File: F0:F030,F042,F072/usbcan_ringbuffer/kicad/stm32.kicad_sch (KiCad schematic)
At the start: 59 parts, among them J1 Screw_Terminal_01x03, J10 SDA, J11 PB0, J12 PB1, J13 PB4, J14 PB5, J15 PB2, J16 PB3, J17 GND, J18 GND, J19 +3.3V, J2 SCK, J20 +5V, J21 PA0, J22 PA1, J23 PA2, J24 PA3, J25 PB10, J26 PB11, J27 PB12, J28 PB13, J29 PB14, J3 SWDetc, J30 PA4, J31 GND, J4 USB_B, J5 MISO, J6 MOSI, J7 TX, J8 RX, J9 SCL, P1 Hole, P2 Hole, P3 Hole, P4 Hole, Q1 B0505S, SW1 SW_DIP_x01, U1 LM1117-3.3, U2 USBLC6-2SC6, U3 STM32F072C8Tx, U4 ISO1050DUB

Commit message: fixed bug with usblc6 on usbcan
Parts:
- removed J27: PB12, TestPoint:TestPoint_THTPad_1.5x1.5mm_Drill0.7mm, symbol Connector:Conn_01x01_Female
- removed J28: PB13, TestPoint:TestPoint_THTPad_1.5x1.5mm_Drill0.7mm, symbol Connector:Conn_01x01_Female
- removed J29: PB14, TestPoint:TestPoint_THTPad_1.5x1.5mm_Drill0.7mm, symbol Connector:Conn_01x01_Female
- removed J30: PA4, TestPoint:TestPoint_THTPad_1.5x1.5mm_Drill0.7mm, symbol Connector:Conn_01x01_Female
- removed J31: GND, TestPoint:TestPoint_THTPad_1.5x1.5mm_Drill0.7mm, symbol Connector:Conn_01x01_Female
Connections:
- net +5V: now also U2.5 (VBUS); no longer U2.2 (GND)
- net GND: now also U2.2 (GND); no longer U2.5 (VBUS)
- net at R3.2: now also U2.4 (I/O2); no longer U2.1 (I/O1)
- net at R4.2: now also U2.6 (I/O1); no longer U2.3 (I/O2)
- net at U3.32 (PA11): now also U2.3 (I/O2); no longer U2.6 (I/O1)
- net at U3.33 (PA12): now also U2.1 (I/O1); no longer U2.4 (I/O2)
- no-connect marks 10 -> 14
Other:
- moved on the sheet: U2
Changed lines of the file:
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@@
   (junction (at 18.161 84.328) (diameter 0) (color 0 0 0 0)
   )
-  (junction (at 102.108 151.257) (diameter 0) (color 0 0 0 0)
+  (junction (at 182.118 138.303) (diameter 0) (color 0 0 0 0)
   )
   (junction (at 118.618 149.098) (diameter 0) (color 0 0 0 0)
@@
   (junction (at 197.104 123.063) (diameter 0) (color 0 0 0 0)
   )
+  (no_connect (at 105.918 138.938))
+  (no_connect (at 105.918 136.398))
   (no_connect (at 105.918 98.298))
   (no_connect (at 138.938 144.018))
@@
   (no_connect (at 105.918 95.758))
   (no_connect (at 105.918 88.138))
+  (no_connect (at 105.918 141.478))
   (no_connect (at 323.85 187.198))
+  (no_connect (at 138.938 116.078))
   (no_connect (at 105.918 90.678))
   (no_connect (at 323.85 193.548))
@@
     (stroke (width 0) (type default) (color 0 0 0 0))
   )
-  (wire (pts (xy 102.108 149.479) (xy 102.108 151.257))
-    (stroke (width 0) (type default) (color 0 0 0 0))
-  )
   (polyline (pts (xy 68.326 45.212) (xy 68.326 14.478))
     (stroke (width 0) (type default) (color 0 0 0 0))
@@
   )
   (label "LED0" (at 105.918 144.018 180)
-    (effects (font (size 1.2 1.2)) (justify right bottom))
+    (effects (font (size 1.524 1.524)) (justify right bottom))
   )
   (label "LED1" (at 21.717 65.659 180)
@@
   )
   (label "CAN_Rx" (at 105.918 126.238 180)
-    (effects (font (size 1.2 1.2)) (justify right bottom))
+    (effects (font (size 1.524 1.524)) (justify right bottom))
   )
   (label "CAN_Tx" (at 85.979 29.083 180)
@@
   )
   (label "LED1" (at 138.938 126.238 0)
-    (effects (font (size 1.2 1.2)) (justify left bottom))
+    (effects (font (size 1.524 1.524)) (justify left bottom))
   )
   (label "BOOT0" (at 136.779 34.925 180)
@@
     (pin "1")
     (pin "2")
+  )
+  (symbol (lib_id "stm32-rescue:PWR_FLAG") (at 182.118 138.303 180) (unit 1)
+    (in_bom yes) (on_board yes)
+    (property "Reference" "#FLG01" (id 0) (at 182.118 140.716 0)
+      (effects (font (size 1.27 1.27)) hide)
+    )
+    (property "Value" "PWR_FLAG" (id 1) (at 182.118 142.875 0)
+      (effects (font (size 1.27 1.27)) hide)
+    )
+    (property "Footprint" "" (id 2) (at 182.118 138.303 0))
+    (property "Datasheet" "" (id 3) (at 182.118 138.303 0))
+    (pin "1")
   )
   (symbol (lib_id "stm32-rescue:R") (at 100.076 86.868 180) (unit 1)
@@
     (pin "1")
   )
-  (symbol (lib_id "Power_Protection:USBLC6-2SC6") (at 167.64 132.969 90) (mirror x) (unit 1)
-    (in_bom yes) (on_board yes)
-    (property "Reference" "U2" (id 0) (at 167.513 117.856 90))
-    (property "Value" "USBLC6-2SC6" (id 1) (at 166.497 120.269 90))
-    (property "Footprint" "Package_TO_SOT_SMD:SOT-23-6_Handsoldering" (id 2) (at 180.34 132.969 0)
-      (effects (font (size 1.27 1.27)) hide)
-    )
-    (property "Datasheet" "https://www.st.com/resource/en/datasheet/usblc6-2.pdf" (id 3) (at 158.75 138.049 0)
+  (symbol (lib_id "Power_Protection:USBLC6-2SC6") (at 167.64 132.969 270) (mirror x) (unit 1)
+    (in_bom yes) (on_board yes)
+    (property "Reference" "U2" (id 0) (at 167.767 148.082 90))
+    (property "Value" "USBLC6-2SC6" (id 1) (at 168.783 145.669 90))
+    (property "Footprint" "Package_TO_SOT_SMD:SOT-23-6_Handsoldering" (id 2) (at 154.94 132.969 0)
+      (effects (font (size 1.27 1.27)) hide)
+    )
+    (property "Datasheet" "https://www.st.com/resource/en/datasheet/usblc6-2.pdf" (id 3) (at 176.53 127.889 0)
       (effects (font (size 1.27 1.27)) hide)
     )
@@
     (pin "1")
   )
-  (symbol (lib_id "Connector:Conn_01x01_Female") (at 100.838 138.938 180) (unit 1)
-    (in_bom yes) (on_board yes)
-    (property "Reference" "J28" (id 0) (at 100.1268 139.7727 0)
-      (effects (font (size 1.27 1.27)) (justify left) hide)
-    )
-    (property "Value" "PB13" (id 1) (at 100.711 138.938 0)
-      (effects (font (size 1.27 1.27)) (justify left))
-    )
-    (property "Footprint" "TestPoint:TestPoint_THTPad_1.5x1.5mm_Drill0.7mm" (id 2) (at 100.838 138.938 0)
-      (effects (font (size 1.27 1.27)) hide)
-    )
-    (property "Datasheet" "~" (id 3) (at 100.838 138.938 0)
-      (effects (font (size 1.27 1.27)) hide)
-    )
-    (pin "1")
-  )
   (symbol (lib_id "Connector:Conn_01x01_Female") (at 144.018 131.318 0) (unit 1)
     (in_bom yes) (on_board yes)
@@
     (pin "1")
   )
-  (symbol (lib_id "Connector:Conn_01x01_Female") (at 144.018 116.078 0) (unit 1)
-    (in_bom yes) (on_board yes)
-    (property "Reference" "J30" (id 0) (at 144.7292 115.2433 0)
-      (effects (font (size 1.27 1.27)) (justify left) hide)
-    )
-    (property "Value" "PA4" (id 1) (at 144.145 116.078 0)
-      (effects (font (size 1.27 1.27)) (justify left))
-    )
-    (property "Footprint" "TestPoint:TestPoint_THTPad_1.5x1.5mm_Drill0.7mm" (id 2) (at 144.018 116.078 0)
-      (effects (font (size 1.27 1.27)) hide)
-    )
-    (property "Datasheet" "~" (id 3) (at 144.018 116.078 0)
-      (effects (font (size 1.27 1.27)) hide)
-    )
-    (pin "1")
-  )
-  (symbol (lib_id "Connector:Conn_01x01_Female") (at 100.838 141.478 180) (unit 1)
-    (in_bom yes) (on_board yes)
-    (property "Reference" "J29" (id 0) (at 100.1268 142.3127 0)
-      (effects (font (size 1.27 1.27)) (justify left) hide)
-    )
-    (property "Value" "PB14" (id 1) (at 100.711 141.478 0)
-      (effects (font (size 1.27 1.27)) (justify left))
-    )
-    (property "Footprint" "TestPoint:TestPoint_THTPad_1.5x1.5mm_Drill0.7mm" (id 2) (at 100.838 141.478 0)
-      (effects (font (size 1.27 1.27)) hide)
-    )
-    (property "Datasheet" "~" (id 3) (at 100.838 141.478 0)
-      (effects (font (size 1.27 1.27)) hide)
-    )
-    (pin "1")
-  )
   (symbol (lib_id "Connector:Conn_01x01_Female") (at 144.018 118.618 0) (unit 1)
     (in_bom yes) (on_board yes)
@@
     )
     (property "Datasheet" "~" (id 3) (at 100.838 131.318 0)
-      (effects (font (size 1.27 1.27)) hide)
-    )
-    (pin "1")
-  )
-  (symbol (lib_id "Connector:Conn_01x01_Female") (at 100.838 136.398 180) (unit 1)
-    (in_bom yes) (on_board yes)
-    (property "Reference" "J27" (id 0) (at 100.1268 137.2327 0)
-      (effects (font (size 1.27 1.27)) (justify left) hide)
-    )
-    (property "Value" "PB12" (id 1) (at 100.711 136.398 0)
-      (effects (font (size 1.27 1.27)) (justify left))
-    )
-    (property "Footprint" "TestPoint:TestPoint_THTPad_1.5x1.5mm_Drill0.7mm" (id 2) (at 100.838 136.398 0)
-      (effects (font (size 1.27 1.27)) hide)
-    )
-    (property "Datasheet" "~" (id 3) (at 100.838 136.398 0)
-      (effects (font (size 1.27 1.27)) hide)
-    )
-    (pin "1")
-  )
-  (symbol (lib_id "Connector:Conn_01x01_Female") (at 97.028 149.479 180) (unit 1)
-    (in_bom yes) (on_board yes)
-    (property "Reference" "J31" (id 0) (at 96.3168 150.3137 0)
-      (effects (font (size 1.27 1.27)) (justify left) hide)
-    )
-    (property "Value" "GND" (id 1) (at 96.901 149.479 0)
-      (effects (font (size 1.27 1.27)) (justify left))
-    )
-    (property "Footprint" "TestPoint:TestPoint_THTPad_1.5x1.5mm_Drill0.7mm" (id 2) (at 97.028 149.479 0)
-      (effects (font (size 1.27 1.27)) hide)
-    )
-    (property "Datasheet" "~" (id 3) (at 97.028 149.479 0)
       (effects (font (size 1.27 1.27)) hide)
     )
@@
   )
   (symbol_instances
+    (path "/00000000-0000-0000-0000-0000590cee5e"
+      (reference "#FLG01") (unit 1) (value "PWR_FLAG") (footprint "")
+    )
     (path "/00000000-0000-0000-0000-000058c45269"
       (reference "#PWR01") (unit 1) (value "+5V") (footprint "")
@@
       (reference "J26") (unit 1) (value "PB11") (footprint "TestPoint:TestPoint_THTPad_1.5x1.5mm_Drill0.7mm")
     )
-    (path "/6acab1d7-5134-4383-9218-96f6aed30a0e"
-      (reference "J27") (unit 1) (value "PB12") (footprint "TestPoint:TestPoint_THTPad_1.5x1.5mm_Drill0.7mm")
-    )
-    (path "/27c8ca30-700e-4f17-a521-c0a04628cef7"
-      (reference "J28") (unit 1) (value "PB13") (footprint "TestPoint:TestPoint_THTPad_1.5x1.5mm_Drill0.7mm")
-    )
-    (path "/5139d6c7-f281-4162-939d-b58b280c93c5"
-      (reference "J29") (unit 1) (value "PB14") (footprint "TestPoint:TestPoint_THTPad_1.5x1.5mm_Drill0.7mm")
-    )
-    (path "/4665fb37-cc57-492c-a310-df271b1f2833"
-      (reference "J30") (unit 1) (value "PA4") (footprint "TestPoint:TestPoint_THTPad_1.5x1.5mm_Drill0.7mm")
-    )
-    (path "/757390d4-03a1-4ffc-88c1-d08120dcec23"
-      (reference "J31") (unit 1) (value "GND") (footprint "TestPoint:TestPoint_THTPad_1.5x1.5mm_Drill0.7mm")
-    )
     (path "/00000000-0000-0000-0000-000059143415"

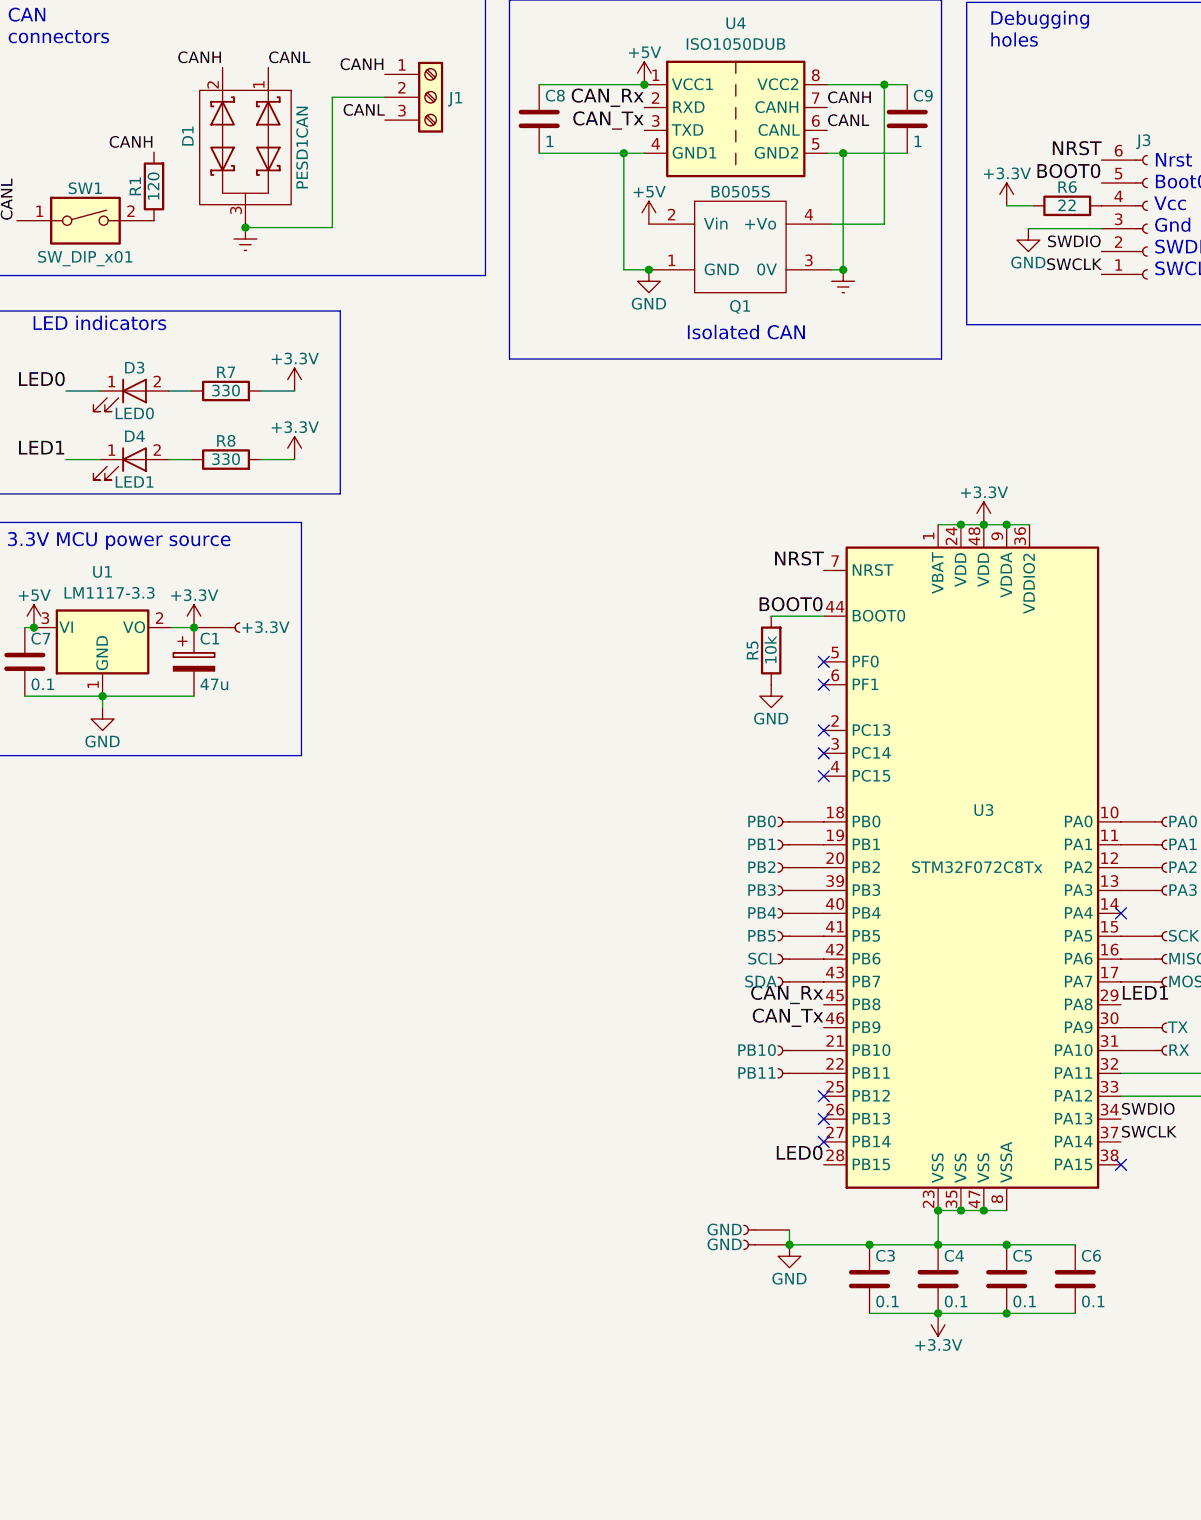
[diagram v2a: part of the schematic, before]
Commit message: -> kicad 8
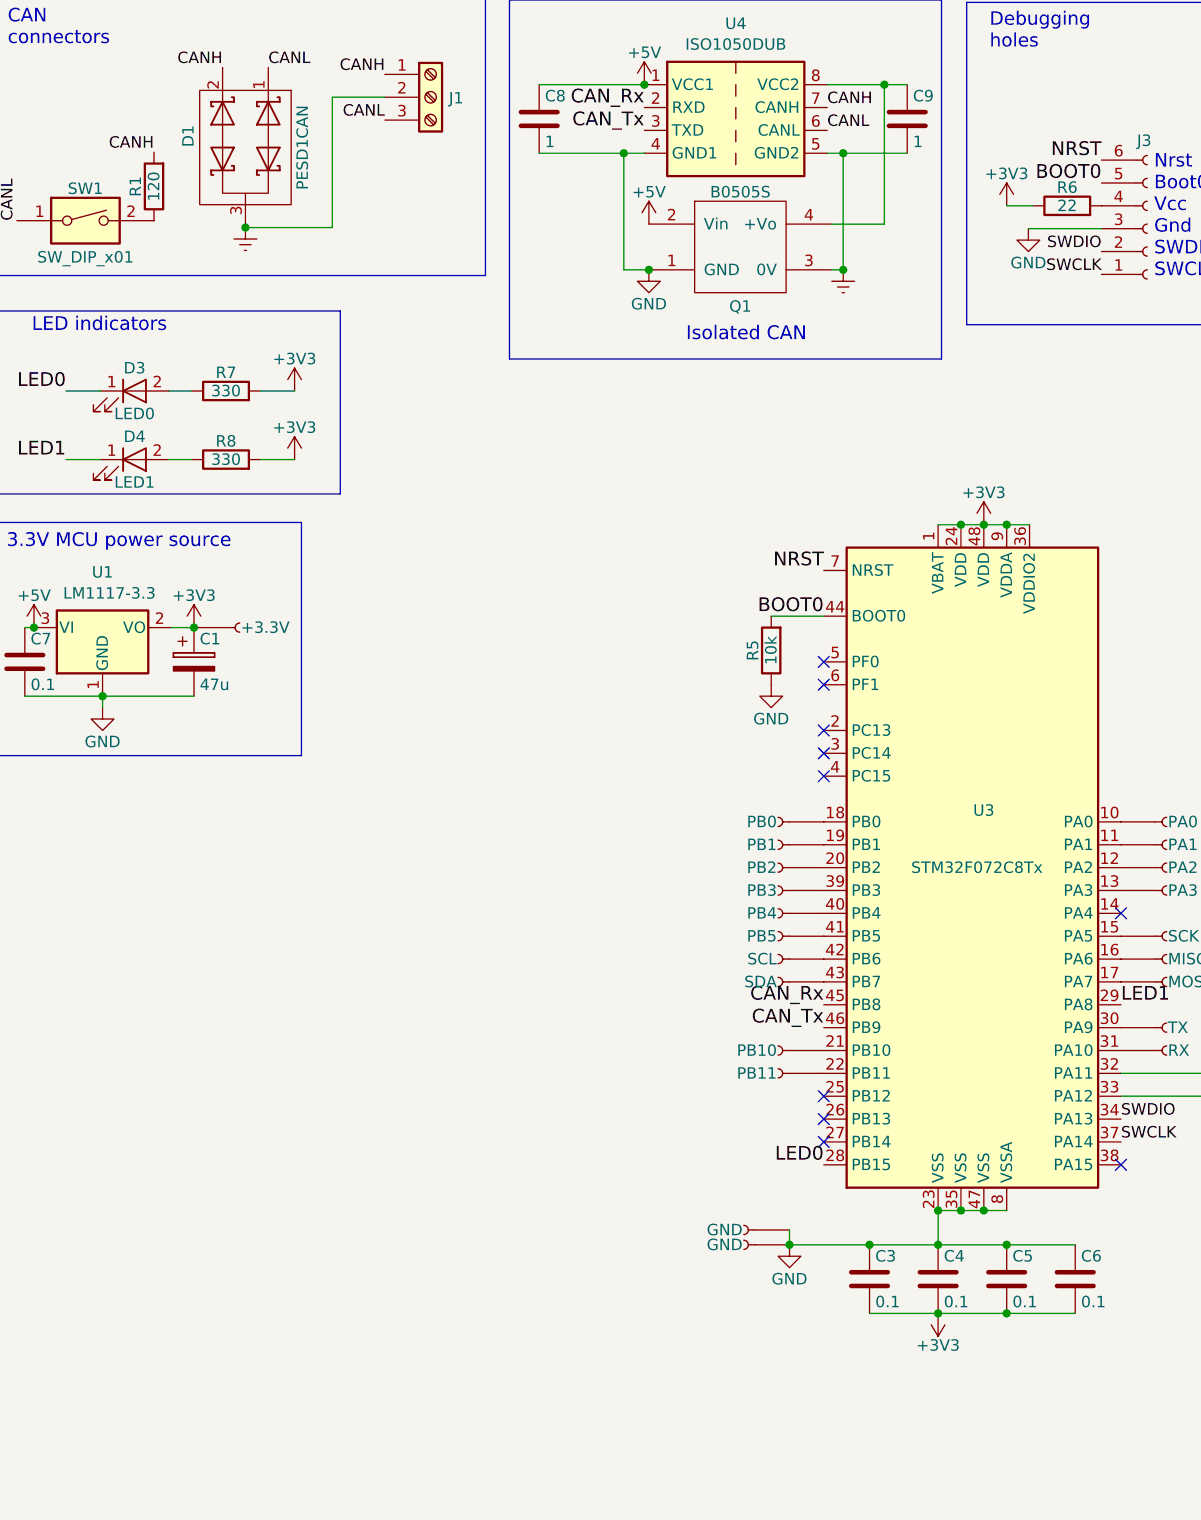
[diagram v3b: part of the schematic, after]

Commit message: starting CAN-GPIO, have a lot of errors
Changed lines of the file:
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@@
 (kicad_sch
-	(version 20231120)
+	(version 20250114)
 	(generator "eeschema")
-	(generator_version "8.0")
+	(generator_version "9.0")
 	(paper "A4")
 	(title_block
@@
 		(company "SAO RAS")
 	)
+	(text "LED indicators"
+		(exclude_from_sim no)
+		(at 17.907 51.689 0)
+		(effects
+			(font
+				(size 1.524 1.524)
+			)
+			(justify left bottom)
+		)
+	)
+	(text "Isolated CAN"
+		(exclude_from_sim no)
+		(at 104.013 52.705 0)
+		(effects
+			(font
+				(size 1.524 1.524)
+			)
+			(justify right bottom)
+		)
+	)
+	(text "Debugging\nholes"
+		(exclude_from_sim no)
+		(at 124.333 20.193 0)
+		(effects
+			(font
+				(size 1.4986 1.4986)
+			)
+			(justify left bottom)
+		)
+	)
+	(text "3.3V MCU power source"
+		(exclude_from_sim no)
+		(at 15.113 75.692 0)
+		(effects
+			(font
+				(size 1.524 1.524)
+			)
+			(justify left bottom)
+		)
+	)
+	(text "Nrst\nBoot0\nVcc\nGnd\nSWDIO\nSWCLK"
+		(exclude_from_sim no)
+		(at 142.621 45.593 0)
+		(effects
+			(font
+				(size 1.4986 1.4986)
+			)
+			(justify left bottom)
+		)
+	)
+	(text "CAN\nconnectors"
+		(exclude_from_sim no)
+		(at 15.24 19.812 0)
+		(effects
+			(font
+				(size 1.4986 1.4986)
+			)
+			(justify left bottom)
+		)
+	)
 	(junction
 		(at 85.979 24.003)
@@
 		)
 	)
-	(text "LED indicators"
-		(exclude_from_sim no)
-		(at 17.907 51.689 0)
-		(effects
-			(font
-				(size 1.524 1.524)
-			)
-			(justify left bottom)
-		)
-	)
-	(text "Isolated CAN"
-		(exclude_from_sim no)
-		(at 104.013 52.705 0)
-		(effects
-			(font
-				(size 1.524 1.524)
-			)
-			(justify right bottom)
-		)
-	)
-	(text "Debugging\nholes"
-		(exclude_from_sim no)
-		(at 124.333 20.193 0)
-		(effects
-			(font
-				(size 1.4986 1.4986)
-			)
-			(justify left bottom)
-		)
-	)
-	(text "3.3V MCU power source"
-		(exclude_from_sim no)
-		(at 15.113 75.692 0)
-		(effects
-			(font
-				(size 1.524 1.524)
-			)
-			(justify left bottom)
-		)
-	)
-	(text "Nrst\nBoot0\nVcc\nGnd\nSWDIO\nSWCLK"
-		(exclude_from_sim no)
-		(at 142.621 45.593 0)
-		(effects
-			(font
-				(size 1.4986 1.4986)
-			)
-			(justify left bottom)
-		)
-	)
-	(text "CAN\nconnectors"
-		(exclude_from_sim no)
-		(at 15.24 19.812 0)
-		(effects
-			(font
-				(size 1.4986 1.4986)
-			)
-			(justify left bottom)
-		)
-	)
 	(label "CANH"
 		(at 106.299 26.543 0)
-		(fields_autoplaced yes)
 		(effects
 			(font
@@
 	(label "CAN_Tx"
 		(at 105.918 128.778 180)
-		(fields_autoplaced yes)
 		(effects
 			(font
@@
 	(label "CANL"
 		(at 16.256 39.116 90)
-		(fields_autoplaced yes)
 		(effects
 			(font
@@
 	(label "CANH"
 		(at 57.15 22.86 180)
-		(fields_autoplaced yes)
 		(effects
 			(font
@@
 	(label "CANL"
 		(at 57.15 27.94 180)
-		(fields_autoplaced yes)
 		(effects
 			(font
@@
 	(label "NRST"
 		(at 136.779 32.385 180)
-		(fields_autoplaced yes)
 		(effects
 			(font
@@
 	(label "LED0"
 		(at 105.918 144.018 180)
-		(fields_autoplaced yes)
 		(effects
 			(font
@@
 	(label "LED1"
 		(at 21.717 65.659 180)
-		(fields_autoplaced yes)
 		(effects
 			(font
@@
 	(label "CANL"
 		(at 106.299 29.083 0)
-		(fields_autoplaced yes)
 		(effects
 			(font
@@
 	(label "SWDIO"
 		(at 138.938 138.938 0)
-		(fields_autoplaced yes)
 		(effects
 			(font
@@
 	(label "CAN_Rx"
 		(at 105.918 126.238 180)
-		(fields_autoplaced yes)
 		(effects
 			(font
@@
 	(label "CAN_Tx"
 		(at 85.979 29.083 180)
-		(fields_autoplaced yes)
 		(effects
 			(font
@@
 	(label "CANL"
 		(at 44.196 22.098 0)
-		(fields_autoplaced yes)
 		(effects
 			(font
@@
 	(label "SWDIO"
 		(at 136.779 42.545 180)
-		(fields_autoplaced yes)
 		(effects
 			(font
@@
 	(label "CANH"
 		(at 39.116 22.098 180)
-		(fields_autoplaced yes)
 		(effects
 			(font
@@
 	(label "LED1"
 		(at 138.938 126.238 0)
-		(fields_autoplaced yes)
 		(effects
 			(font
@@
 	(label "BOOT0"
 		(at 136.779 34.925 180)
-		(fields_autoplaced yes)
 		(effects
 			(font
@@
 	(label "SWCLK"
 		(at 136.779 45.085 180)
-		(fields_autoplaced yes)
 		(effects
 			(font
@@
 	(label "BOOT0"
 		(at 105.918 83.058 180)
-		(fields_autoplaced yes)
 		(effects
 			(font
@@
 	(label "CANH"
 		(at 31.496 31.496 180)
-		(fields_autoplaced yes)
 		(effects
 			(font
@@
 	(label "SWCLK"
 		(at 138.938 141.478 0)
-		(fields_autoplaced yes)
 		(effects
 			(font
@@
 	(label "CAN_Rx"
 		(at 85.979 26.543 180)
-		(fields_autoplaced yes)
 		(effects
 			(font
@@
 	(label "NRST"
 		(at 105.918 77.978 180)
-		(fields_autoplaced yes)
 		(effects
 			(font
@@
 	(label "LED0"
 		(at 21.717 58.039 180)
-		(fields_autoplaced yes)
 		(effects
 			(font
@@
 		)
 	)
+	(embedded_fonts no)
 )
